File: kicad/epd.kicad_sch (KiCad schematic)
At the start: 19 parts, among them Q401 Si1308EDL

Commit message: Begin PCB, update footprints
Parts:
- C401, C403: footprint Capacitor_SMD:C_0805_2012Metric_Pad1.18x1.45mm_HandSolder -> Capacitor_SMD:C_0805_2012Metric
- C402, C404, C405, C406, C407, C408, C409: footprint Capacitor_SMD:C_0805_2012Metric_Pad1.18x1.45mm_HandSolder -> Capacitor_SMD:C_0402_1005Metric
- R401, R402, R403, R404: footprint Resistor_SMD:R_0603_1608Metric_Pad0.98x0.95mm_HandSolder -> Resistor_SMD:R_0402_1005Metric
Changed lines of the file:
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@@
 			)
 		)
-		(property "Footprint" "Capacitor_SMD:C_0805_2012Metric_Pad1.18x1.45mm_HandSolder"
+		(property "Footprint" "Capacitor_SMD:C_0402_1005Metric"
 			(at 184.15 109.5248 0)
 			(effects
@@
 			)
 		)
-		(property "Footprint" "Capacitor_SMD:C_0805_2012Metric_Pad1.18x1.45mm_HandSolder"
+		(property "Footprint" "Capacitor_SMD:C_0402_1005Metric"
 			(at 141.2748 62.23 0)
 			(effects
@@
 			)
 		)
-		(property "Footprint" "Resistor_SMD:R_0603_1608Metric_Pad0.98x0.95mm_HandSolder"
+		(property "Footprint" "Resistor_SMD:R_0402_1005Metric"
 			(at 94.742 73.66 90)
 			(effects
@@
 			)
 		)
-		(property "Footprint" "Capacitor_SMD:C_0805_2012Metric_Pad1.18x1.45mm_HandSolder"
+		(property "Footprint" "Capacitor_SMD:C_0402_1005Metric"
 			(at 184.15 104.4448 0)
 			(effects
@@
 			)
 		)
-		(property "Footprint" "Capacitor_SMD:C_0805_2012Metric_Pad1.18x1.45mm_HandSolder"
+		(property "Footprint" "Capacitor_SMD:C_0402_1005Metric"
 			(at 184.15 94.2848 0)
 			(effects
@@
 			)
 		)
-		(property "Footprint" "Resistor_SMD:R_0603_1608Metric_Pad0.98x0.95mm_HandSolder"
+		(property "Footprint" "Resistor_SMD:R_0402_1005Metric"
 			(at 89.408 67.31 90)
 			(effects
@@
 			)
 		)
-		(property "Footprint" "Capacitor_SMD:C_0805_2012Metric_Pad1.18x1.45mm_HandSolder"
+		(property "Footprint" "Capacitor_SMD:C_0805_2012Metric"
 			(at 128.27 54.3052 0)
 			(effects
@@
 			)
 		)
-		(property "Footprint" "Resistor_SMD:R_0603_1608Metric_Pad0.98x0.95mm_HandSolder"
+		(property "Footprint" "Resistor_SMD:R_0402_1005Metric"
 			(at 164.592 83.82 90)
 			(effects
@@
 			)
 		)
-		(property "Footprint" "Capacitor_SMD:C_0805_2012Metric_Pad1.18x1.45mm_HandSolder"
+		(property "Footprint" "Capacitor_SMD:C_0402_1005Metric"
 			(at 118.4148 62.23 0)
 			(effects
@@
 			)
 		)
-		(property "Footprint" "Capacitor_SMD:C_0805_2012Metric_Pad1.18x1.45mm_HandSolder"
+		(property "Footprint" "Capacitor_SMD:C_0805_2012Metric"
 			(at 82.2452 55.88 0)
 			(effects
@@
 			)
 		)
-		(property "Footprint" "Capacitor_SMD:C_0805_2012Metric_Pad1.18x1.45mm_HandSolder"
+		(property "Footprint" "Capacitor_SMD:C_0402_1005Metric"
 			(at 191.77 61.2648 0)
 			(effects
@@
 			)
 		)
-		(property "Footprint" "Resistor_SMD:R_0603_1608Metric_Pad0.98x0.95mm_HandSolder"
+		(property "Footprint" "Resistor_SMD:R_0402_1005Metric"
 			(at 153.162 83.82 90)
 			(effects
@@
 			)
 		)
-		(property "Footprint" "Capacitor_SMD:C_0805_2012Metric_Pad1.18x1.45mm_HandSolder"
+		(property "Footprint" "Capacitor_SMD:C_0402_1005Metric"
 			(at 184.15 99.3648 0)
 			(effects

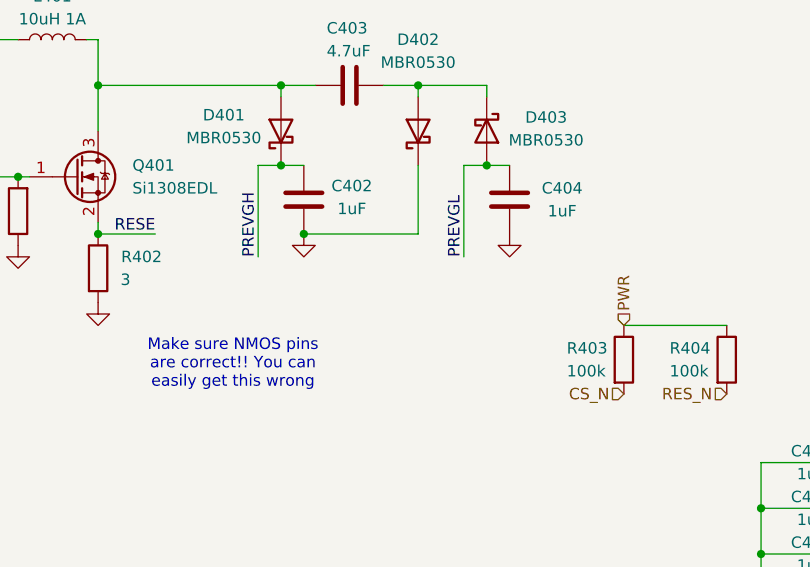
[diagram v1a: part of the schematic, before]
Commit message: Update PCB for better routing of RF, USB-C, and through backside
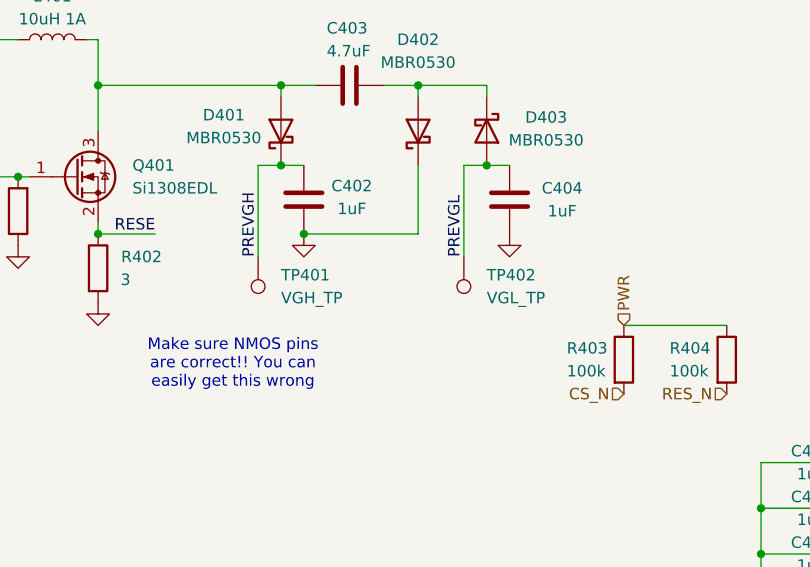
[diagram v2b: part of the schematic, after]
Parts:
- added TP401: VGH_TP, TestPoint:TestPoint_Pad_D1.0mm, symbol Connector:TestPoint
- added TP402: VGL_TP, TestPoint:TestPoint_Pad_D1.0mm, symbol Connector:TestPoint
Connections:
- net PREVGH: now also TP401.1
- net PREVGL: now also TP402.1
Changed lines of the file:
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@@
+	)
+	(symbol
+		(lib_id "Connector:TestPoint")
+		(at 137.16 72.39 180)
+		(unit 1)
+		(exclude_from_sim no)
+		(in_bom yes)
+		(on_board yes)
+		(dnp no)
+		(fields_autoplaced yes)
+		(property "Reference" "TP402"
+			(at 139.7 74.4219 0)
+			(effects
+				(font
+					(size 1.27 1.27)
+				)
+				(justify right)
+			)
+		)
+		(property "Value" "VGL_TP"
+			(at 139.7 76.9619 0)
+			(effects
+				(font
+					(size 1.27 1.27)
+				)
+				(justify right)
+			)
+		)
+		(property "Footprint" "TestPoint:TestPoint_Pad_D1.0mm"
+			(at 132.08 72.39 0)
+			(effects
+				(font
+					(size 1.27 1.27)
+				)
+				(hide yes)
+			)
+		)
+		(property "Datasheet" "~"
+			(at 132.08 72.39 0)
+			(effects
+				(font
+					(size 1.27 1.27)
+				)
+				(hide yes)
+			)
+		)
+		(property "Description" "test point"
+			(at 137.16 72.39 0)
+			(effects
+				(font
+					(size 1.27 1.27)
+				)
+				(hide yes)
+			)
+		)
+		(pin "1"
+		)
+		(instances
+			(project "kicad"
+				(path "/97e37379-fec6-4f0d-82d9-4ea53516bb02/0b88743c-b183-4be0-afee-bdc67a5fc676"
+					(reference "TP402")
+					(unit 1)
+				)
+			)
+		)
 	)
 	(symbol
@@
 					(unit 1)
 				)
+			)
+		)
+	)
+	(symbol
+		(lib_id "Connector:TestPoint")
+		(at 114.3 72.39 180)
+		(unit 1)
+		(exclude_from_sim no)
+		(in_bom yes)
+		(on_board yes)
+		(dnp no)
+		(fields_autoplaced yes)
+		(property "Reference" "TP401"
+			(at 116.84 74.4219 0)
+			(effects
+				(font
+					(size 1.27 1.27)
+				)
+				(justify right)
+			)
+		)
+		(property "Value" "VGH_TP"
+			(at 116.84 76.9619 0)
+			(effects
+				(font
+					(size 1.27 1.27)
+				)
+				(justify right)
+			)
+		)
+		(property "Footprint" "TestPoint:TestPoint_Pad_D1.0mm"
+			(at 109.22 72.39 0)
+			(effects
+				(font
+					(size 1.27 1.27)
+				)
+				(hide yes)
+			)
+		)
+		(property "Datasheet" "~"
+			(at 109.22 72.39 0)
+			(effects
+				(font
+					(size 1.27 1.27)
+				)
+				(hide yes)
+			)
+		)
+		(property "Description" "test point"
+			(at 114.3 72.39 0)
+			(effects
+				(font
+					(size 1.27 1.27)
+				)
+				(hide yes)
+			)
+		)
+		(pin "1"
+		)
+		(instances
+			(project "kicad"
+				(path "/97e37379-fec6-4f0d-82d9-4ea53516bb02/0b88743c-b183-4be0-afee-bdc67a5fc676"
+					(reference "TP401")
+					(unit 1)
+				)

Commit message: Begin EPD redo
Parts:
- EPD_FPC401: footprint Raven:CONN_F3311A7H121024E200_AMP -> Raven:CONN_F3311A7H121024E200_AMP_FACE_UP
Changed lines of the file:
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@@
 		(on_board yes)
 		(dnp no)
-		(fields_autoplaced yes)
 		(property "Reference" "EPD_FPC401"
 			(at 205.74 80.0099 0)
@@
 			)
 		)
-		(property "Footprint" "Raven:CONN_F3311A7H121024E200_AMP"
+		(property "Footprint" "Raven:CONN_F3311A7H121024E200_AMP_FACE_UP"
 			(at 196.85 80.01 0)
 			(effects

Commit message: v2.0.1
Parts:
- removed TP401: VGH_TP, TestPoint:TestPoint_Pad_D1.0mm, symbol Connector:TestPoint
- removed TP402: VGL_TP, TestPoint:TestPoint_Pad_D1.0mm, symbol Connector:TestPoint
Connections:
- net PREVGH: no longer C402.2, D401.1 (K)
- net PREVGL: no longer C404.2, D403.2 (A)
- new net: C404.2, D403.2 (A)
- new net: C402.2, D401.1 (K)
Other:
- moved on the sheet: C402, C404

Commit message: v2.0.2
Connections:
- net PREVGH: now also C402.2, D401.1 (K)
- net PREVGL: now also C404.2, D403.2 (A)
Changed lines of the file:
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@@
 	(title_block
 		(title "E-Paper Display Module")
-		(date "2025-01-27")
+		(date "2025-05-08")
 		(rev "2")
 		(company "Mosaic Labs")
 		(comment 1 "Lucas Merritt")
-		(comment 2 "Rev. 2 verified")
-		(comment 3 "Final ready")
+	)
+	(junction
+		(at 139.7 62.23)
+		(diameter 0)
+		(color 0 0 0 0)
 	)
 	(junction
@@
 	)
 	(junction
+		(at 116.84 62.23)
+		(diameter 0)
+		(color 0 0 0 0)
+	)
+	(junction
 		(at 132.08 53.34)
 		(diameter 0)
@@
 	(wire
 		(pts
+			(xy 111.76 71.12) (xy 111.76 62.23)
+		)
+		(stroke
+			(width 0)
+			(type default)
+		)
+	)
+	(wire
+		(pts
 			(xy 116.84 69.85) (xy 132.08 69.85)
 		)
@@
 	(wire
 		(pts
+			(xy 135.89 62.23) (xy 139.7 62.23)
+		)
+		(stroke
+			(width 0)
+			(type default)
+		)
+	)
+	(wire
+		(pts
 			(xy 191.77 88.9) (xy 191.77 90.17)
 		)
@@
 	(wire
 		(pts
+			(xy 135.89 71.12) (xy 135.89 62.23)
+		)
+		(stroke
+			(width 0)
+			(type default)
+		)
+	)
+	(wire
+		(pts
 			(xy 81.28 63.5) (xy 87.63 63.5)
 		)
@@
 		(pts
 			(xy 179.07 62.23) (xy 184.15 62.23)
+		)
+		(stroke
+			(width 0)
+			(type default)
+		)
+	)
+	(wire
+		(pts
+			(xy 111.76 62.23) (xy 116.84 62.23)
 		)
 		(stroke
@@
 		)
 	)
+	(label "PREVGL"
+		(at 135.89 71.12 90)
+		(fields_autoplaced yes)
+		(effects
+			(font
+				(size 1.27 1.27)
+			)
+			(justify left bottom)
+		)
+	)
 	(label "PREVGH"
 		(at 182.88 102.87 0)
@@
 	(label "PREVGL"
 		(at 182.88 107.95 0)
+		(fields_autoplaced yes)
+		(effects
+			(font
+				(size 1.27 1.27)
+			)
+			(justify left bottom)
+		)
+	)
+	(label "PREVGH"
+		(at 111.76 71.12 90)
 		(fields_autoplaced yes)
 		(effects
@@
 		(on_board yes)
 		(dnp no)
-		(fields_autoplaced yes)
 		(property "Reference" "Q401"
-			(at 100.33 62.2299 0)
+			(at 99.06 60.96 0)
 			(effects
 				(font
@@
 		)
 		(property "Value" "Si1308EDL"
-			(at 100.33 64.7699 0)
+			(at 99.06 63.5 0)
 			(effects
 				(font

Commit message: start v3, complete pcb restart and remove haptics
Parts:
- D401, D402, D403: footprint Diode_SMD:D_SOD-123 -> Raven:NSR05F40NXT5G
- renumbered C403 to C402, C409 to C403, C402 to C404, C404 to C405, C405 to C406, C406 to C407, C407 to C408, C408 to C409
